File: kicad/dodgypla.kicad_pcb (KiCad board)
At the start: 2 copper layers, 19 x 36.8 mm, 8 parts, among them J1 PLA_Conn, J2 JTAG, U1 AMS1117, U2 XC9536XL

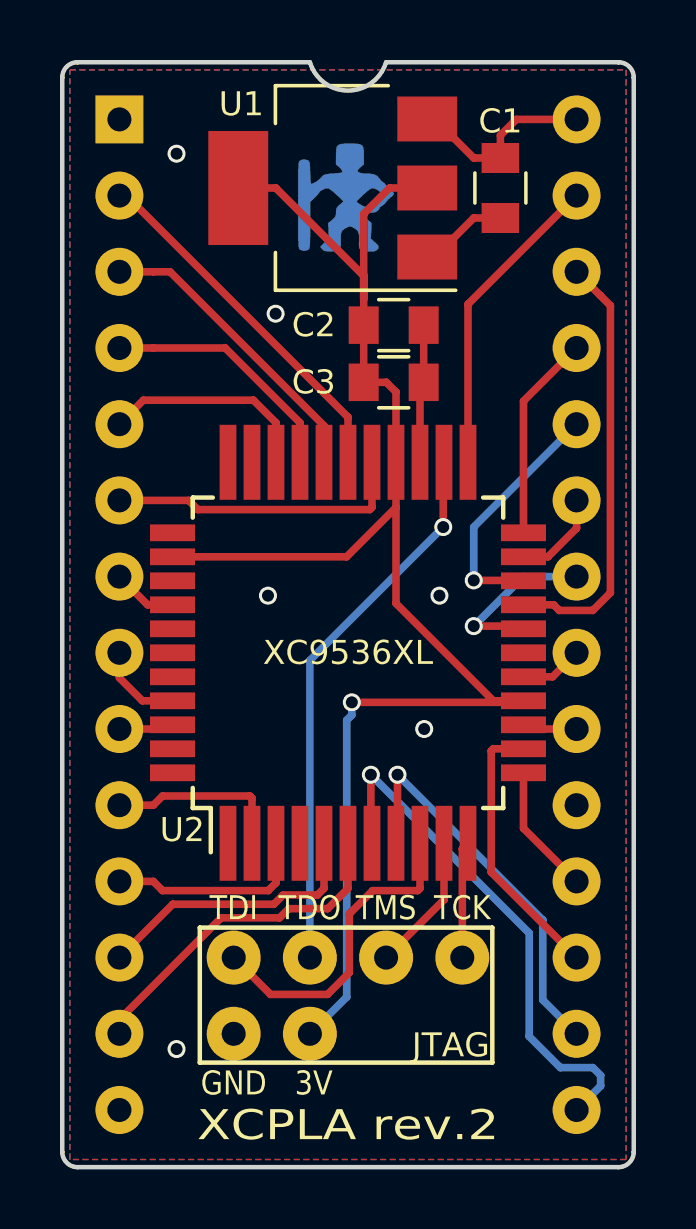
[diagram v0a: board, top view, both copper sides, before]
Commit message: Added missing bypass caps.
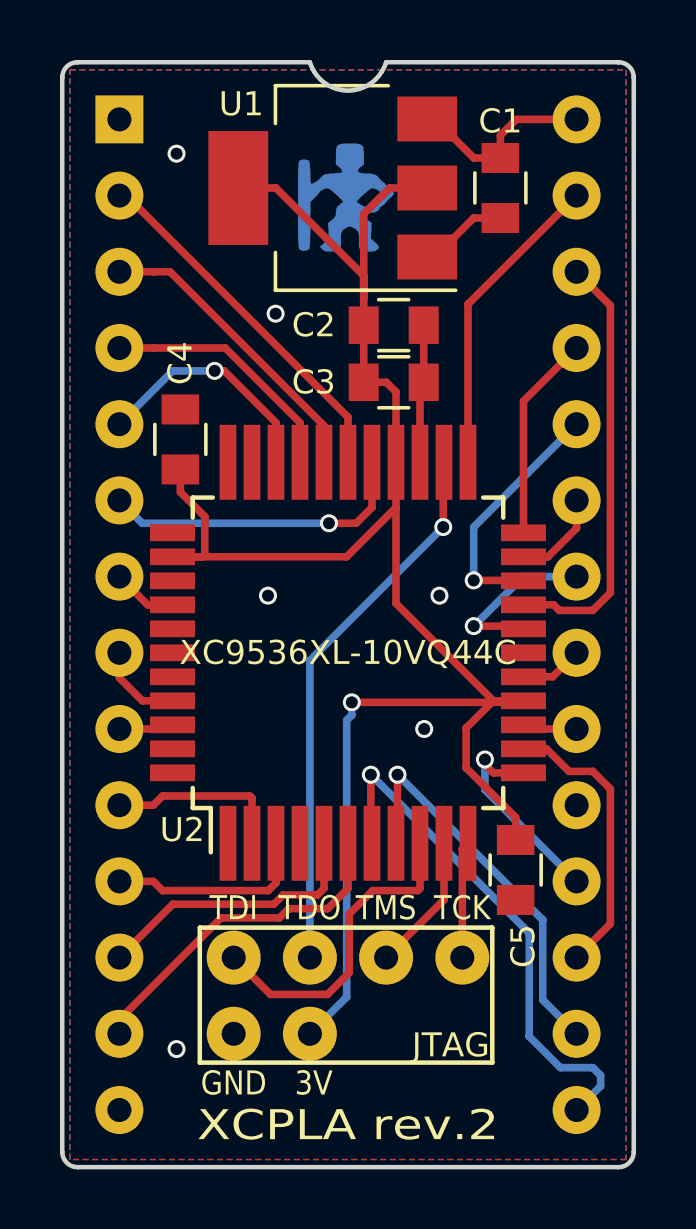
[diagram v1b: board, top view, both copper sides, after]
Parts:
- added C4: 0.1uF, Capacitors_SMD:C_0805, F.Cu at (125.9, 91.6)
- added C5: 0.1uF, Capacitors_SMD:C_0805, F.Cu at (137.0, 105.9)
- U2: value XC9536XL -> XC9536XL-10VQ44C
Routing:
- net +3V3: track 53.6 -> 63.6 mm
- net /PLA_CASRAM: track 4.35 -> 6.89 mm, vias 0 -> 1
- net /PLA_VA14: track 7.18 -> 7.99 mm, vias 0 -> 1
- net /PLA_CHAREN: track 10.1 -> 10.5 mm, vias 0 -> 1

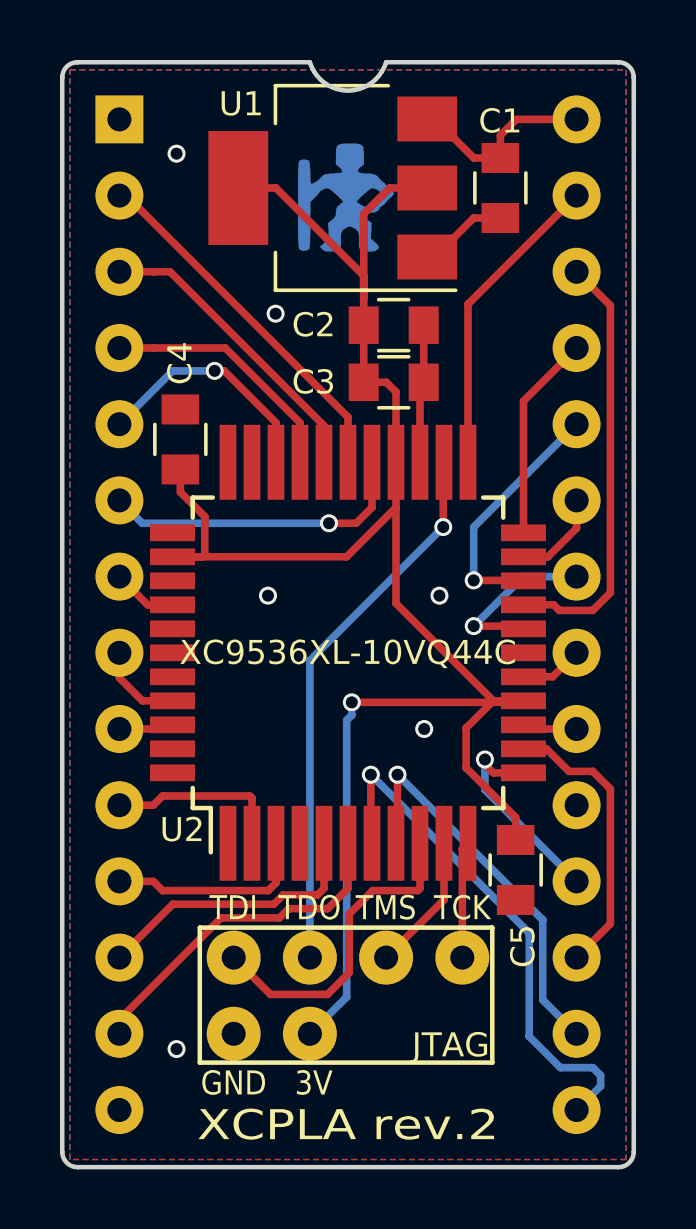
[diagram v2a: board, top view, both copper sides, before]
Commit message: Use LQFP44 standard footprint.
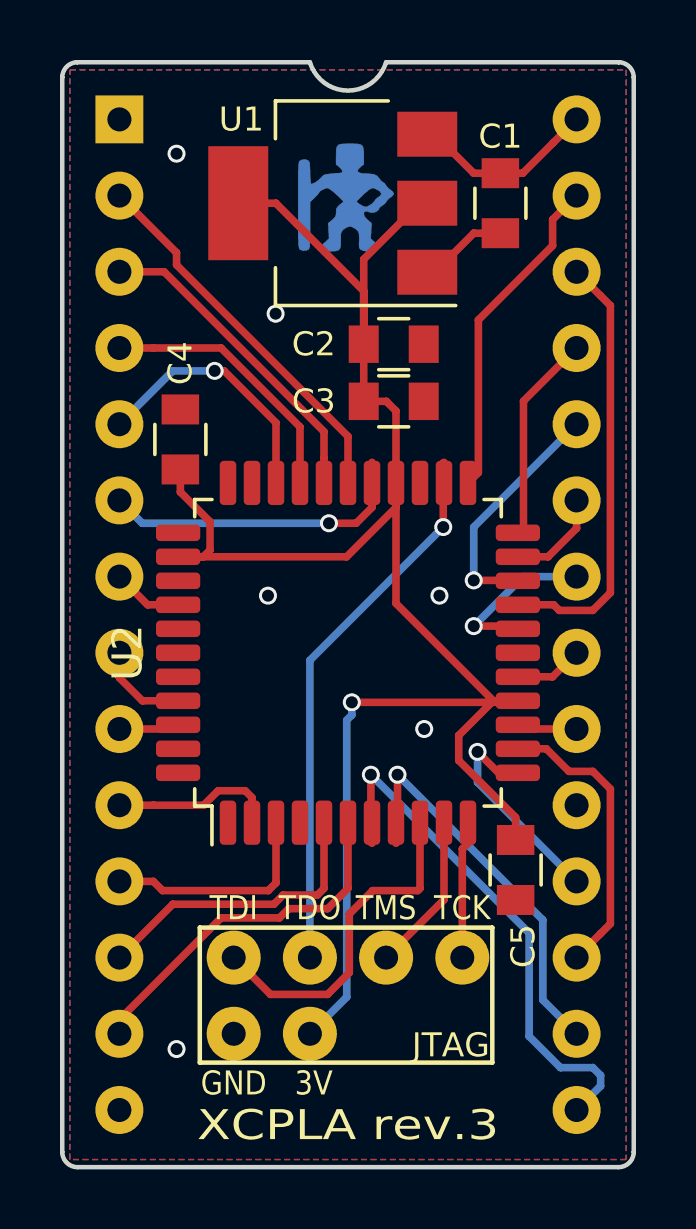
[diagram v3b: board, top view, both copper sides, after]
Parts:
- U2: footprint dodgyPLA_footprints:LQFP-44_10x10mm_Pitch0.8mm -> Package_QFP:LQFP-44_10x10mm_P0.8mm
- moved C2 0.63 mm to (133.0, 88.4)
- moved C3 0.63 mm to (133.0, 90.3)
- moved C1 0.51 mm to (136.5, 83.7)
- moved U1 0.51 mm to (130.9, 83.7)
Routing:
- net GND: track 7.60 -> 2.98 mm
- net +3V3: track 63.6 -> 64.4 mm
- net /PLA_A12: track 10.4 -> 11.1 mm
- net /PLA_A15: track 8.37 -> 8.98 mm
- net /PLA_A14: track 10.2 -> 10.7 mm
- net /PLA_A13: track 12.2 -> 12.7 mm
- net /PLA_ROMH: track 6.08 -> 5.55 mm
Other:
- board text added: "XCPLA rev.3"
- board text removed: "XCPLA rev.2"

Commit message: Smaller THT pads and solder mask clearance.
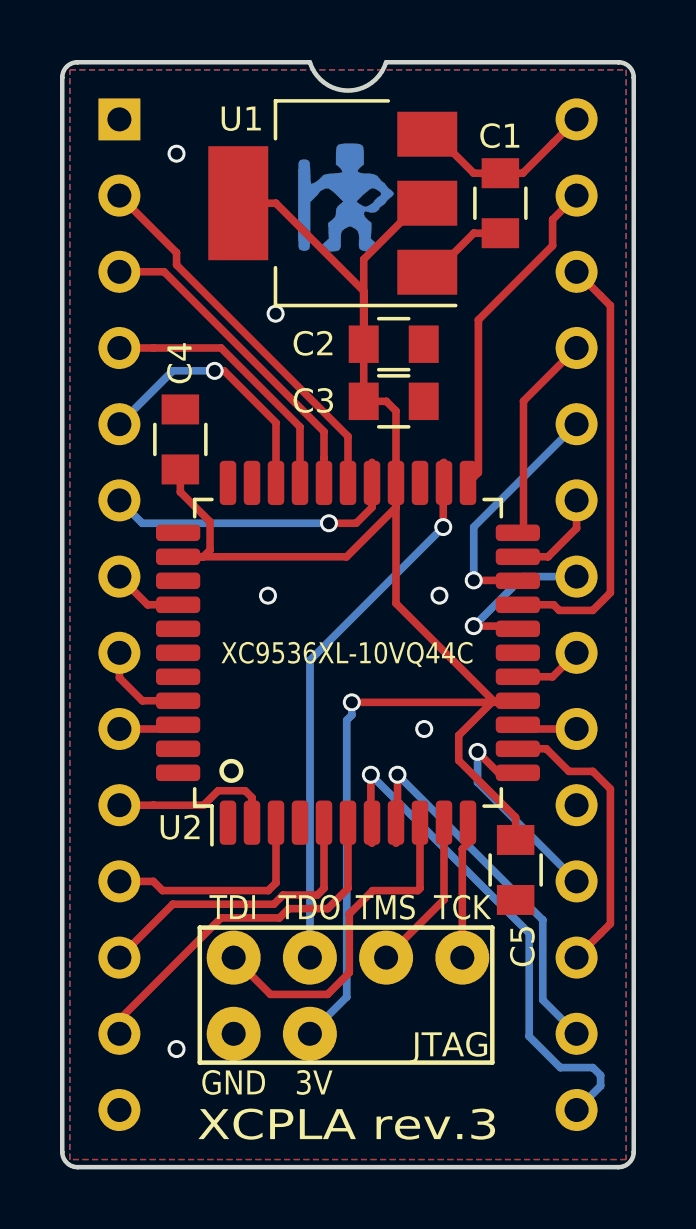
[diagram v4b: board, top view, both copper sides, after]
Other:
- rule pad_to_mask_clearance: 0.2 -> 0.15
